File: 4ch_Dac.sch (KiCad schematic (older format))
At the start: 4 parts, among them J13 Conn_Coaxial, J14 Conn_Coaxial, J15 Conn_Coaxial, J16 Conn_Coaxial

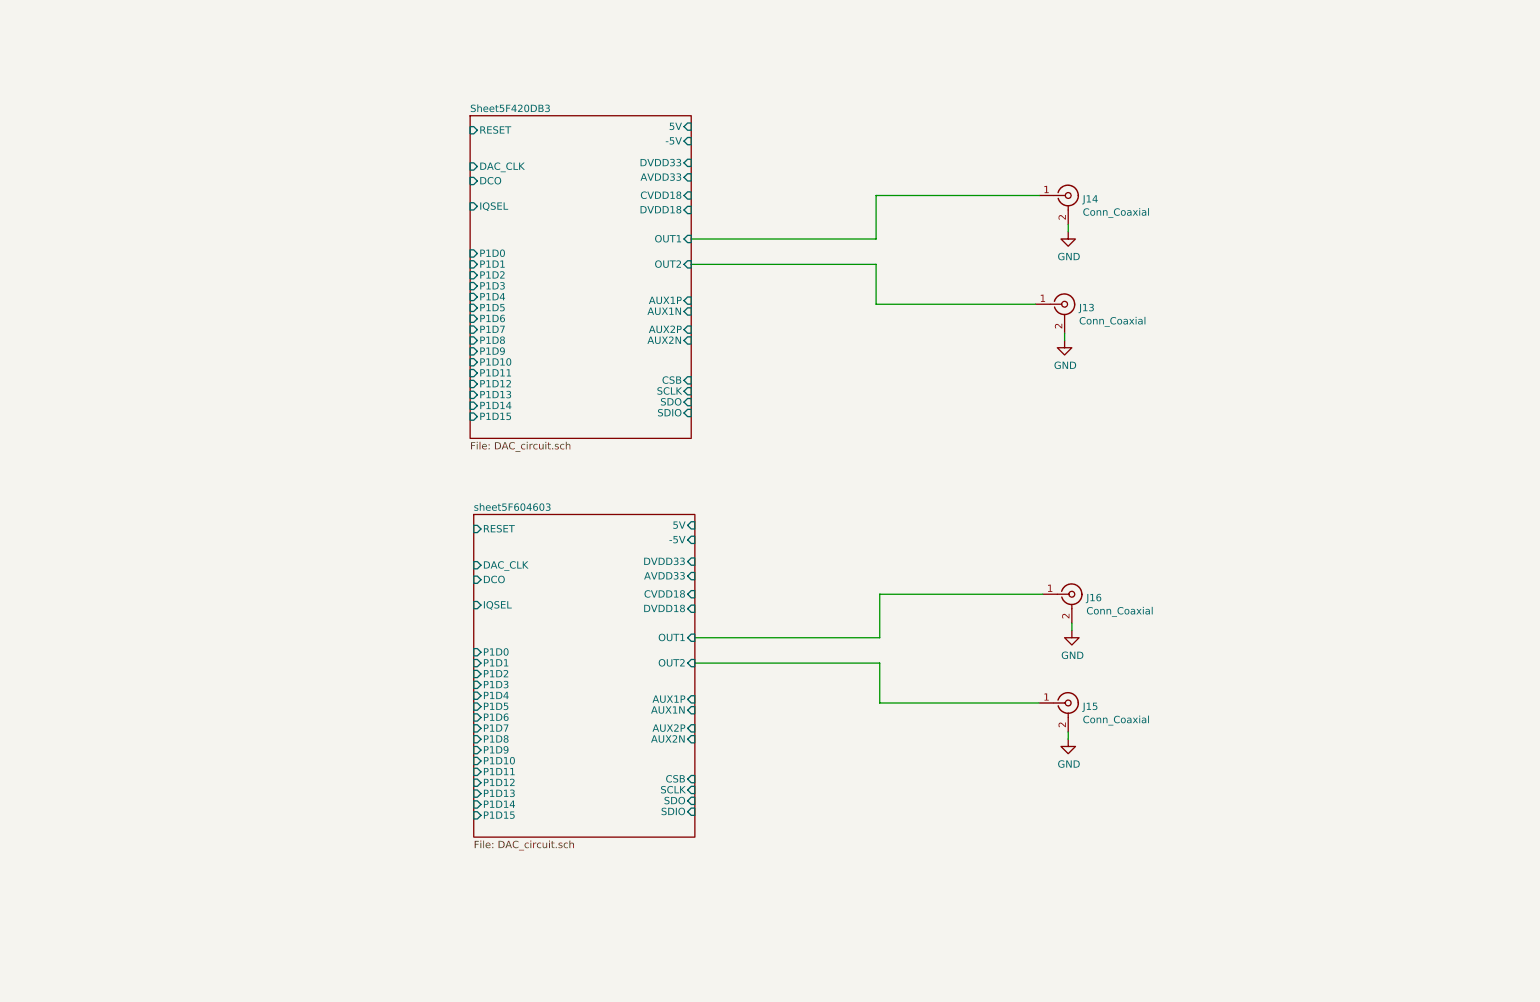
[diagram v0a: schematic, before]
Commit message: initial placement of all ADC/DAC blocks and added FPGA
Signed-off-by: Alexis Jeandet <alexis.jeandet@member.fsf.org>
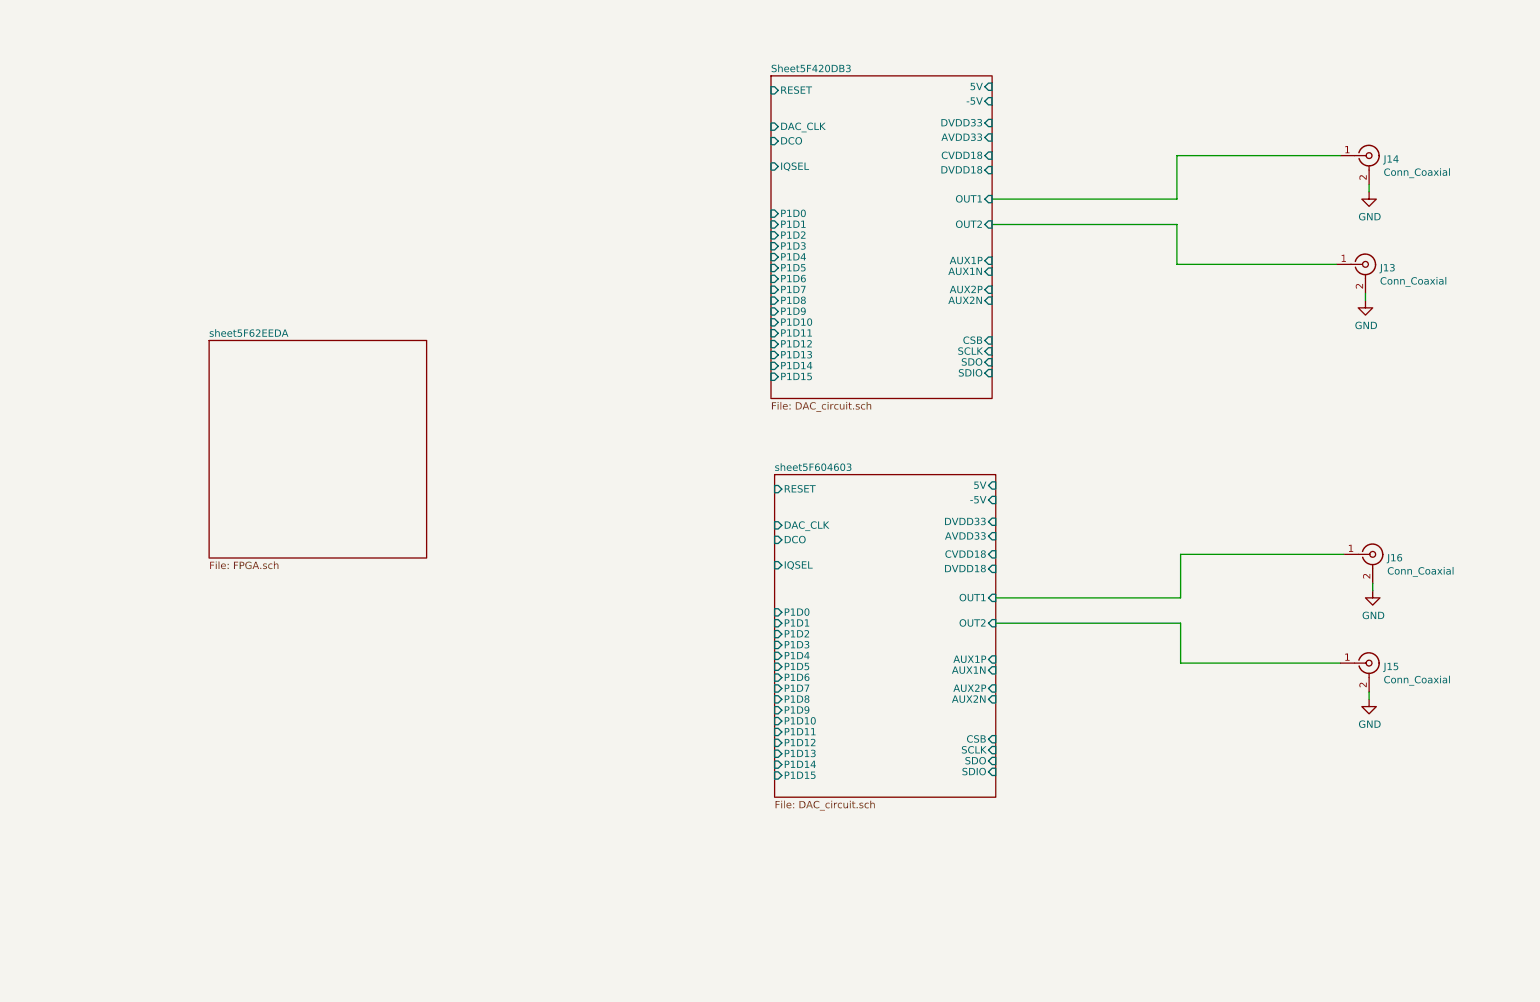
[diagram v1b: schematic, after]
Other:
- moved on the sheet: J13, J14, J15, J16

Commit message: Layout done for ADC + LVDS and DAC -> FPGA
Signed-off-by: Alexis Jeandet <alexis.jeandet@member.fsf.org>
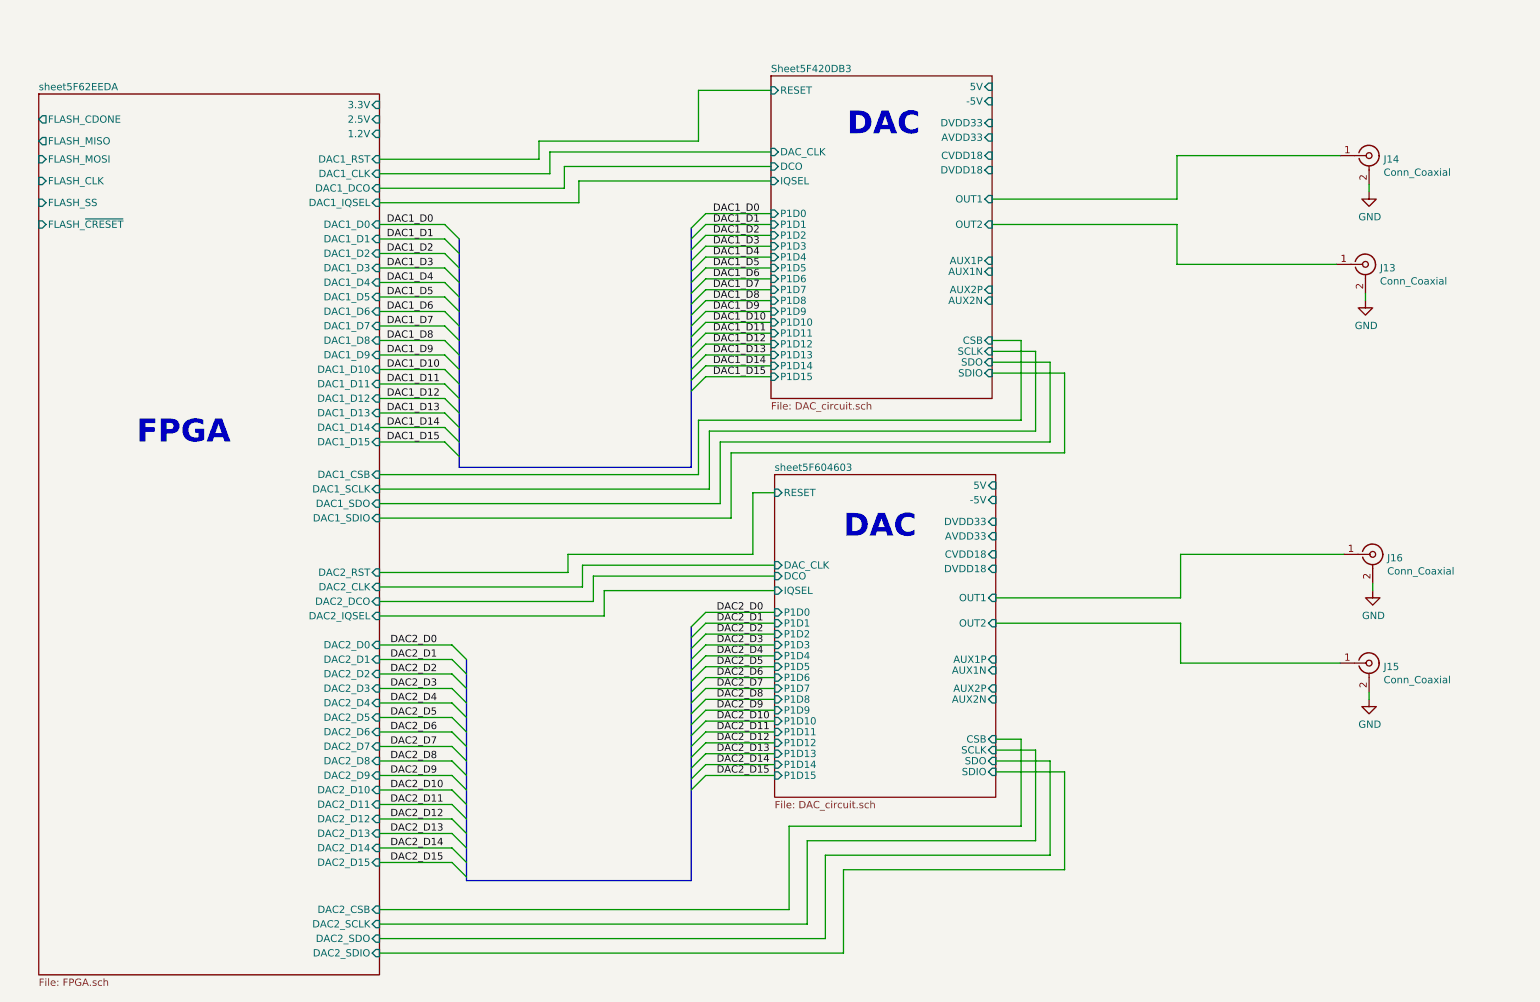
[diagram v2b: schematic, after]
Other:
- note added: "DAC"
- note added: "FPGA"

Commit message: Added #3.3V and #1.2V supply, completed ADC to USB board layout, added DAC FPGA to USB board bus.
Signed-off-by: Alexis Jeandet <alexis.jeandet@member.fsf.org>
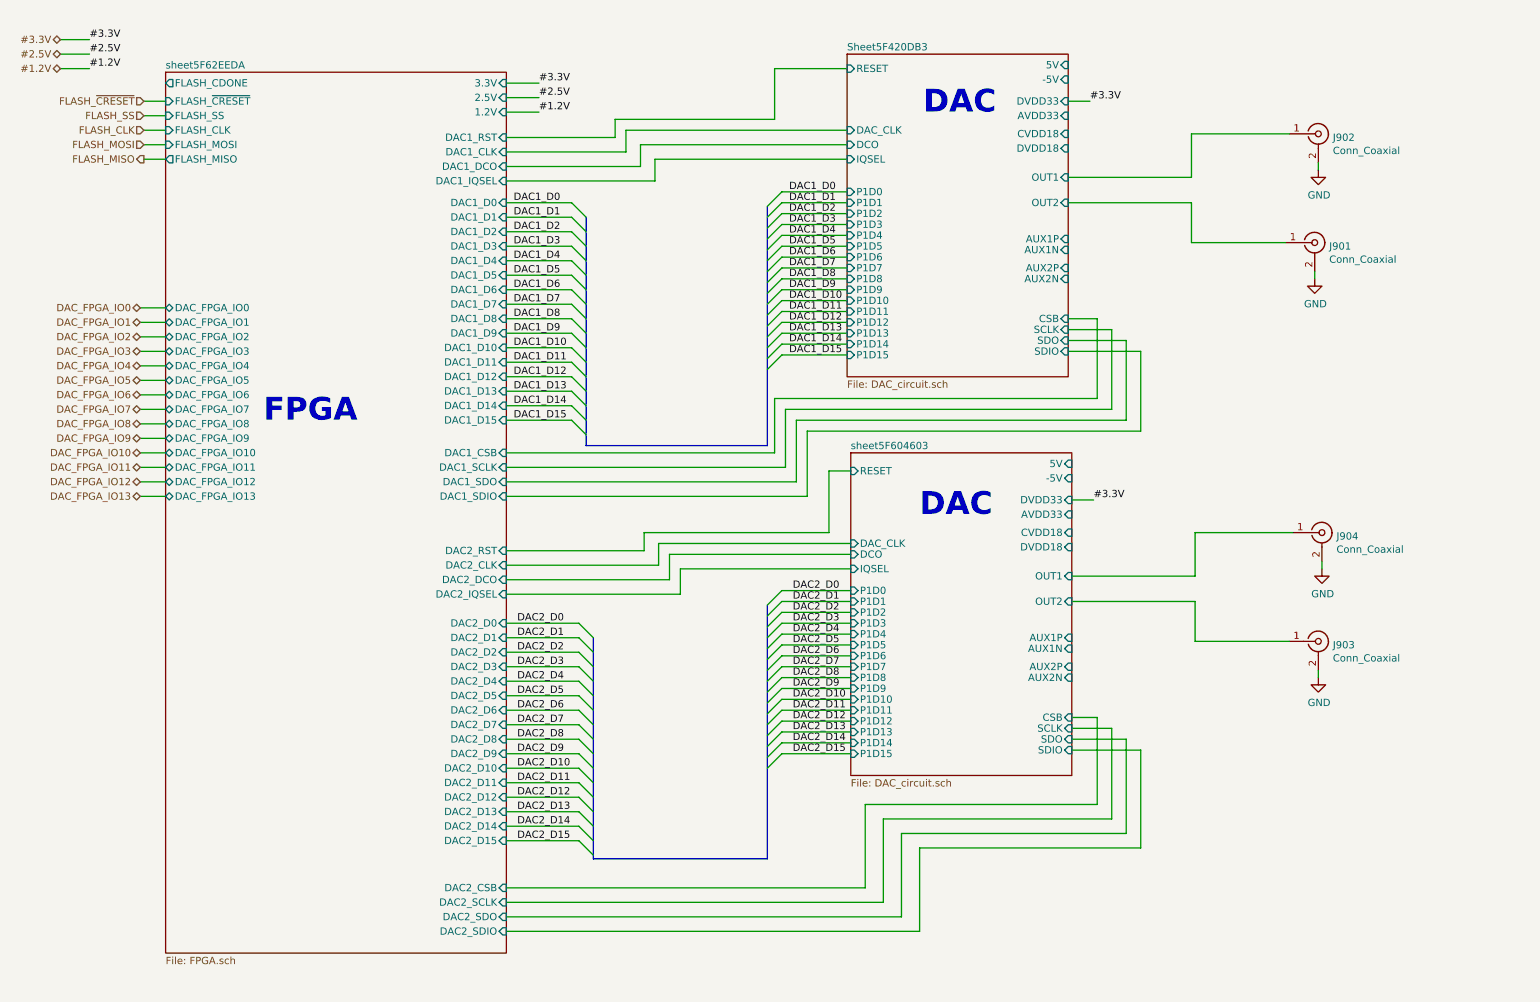
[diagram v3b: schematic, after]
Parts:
- renumbered J13 to J901, J14 to J902, J15 to J903, J16 to J904
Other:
- moved on the sheet: J901, J902, J903, J904

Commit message: Layout complete, needs silk screen cleanup and few checks
Signed-off-by: Alexis Jeandet <alexis.jeandet@member.fsf.org>
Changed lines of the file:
@@
 Wire Wire Line
 	1675 3850 1500 3850
-Text HLabel 950  700  0    50   BiDi ~ 0
+Text HLabel 10600 600  0    50   BiDi ~ 0
 #3.3V
-Text HLabel 950  800  0    50   BiDi ~ 0
+Text HLabel 10600 700  0    50   BiDi ~ 0
 #2.5V
-Text HLabel 950  900  0    50   BiDi ~ 0
+Text HLabel 10600 900  0    50   BiDi ~ 0
 #1.2V
 Wire Wire Line
-	950  700  1150 700
+	10600 600  10800 600
 Wire Wire Line
-	950  800  1150 800
+	10600 700  10800 700
 Wire Wire Line
-	950  900  1150 900
-Text Label 1150 700  0    50   ~ 0
+	10600 900  10800 900
+Text Label 10800 600  0    50   ~ 0
 #3.3V
-Text Label 1150 800  0    50   ~ 0
+Text Label 10800 700  0    50   ~ 0
 #2.5V
-Text Label 1150 900  0    50   ~ 0
+Text Label 10800 900  0    50   ~ 0
 #1.2V
 Text Label 4250 1000 0    50   ~ 0
@@
 Wire Wire Line
 	7900 1125 8050 1125
-Text Label 8075 3875 0    50   ~ 0
-#3.3V
-Wire Wire Line
-	7925 3875 8075 3875
 Text HLabel 1525 1525 0    50   Output ~ 0
 FLASH_MISO
@@
 Wire Wire Line
 	1675 1525 1525 1525
+Text Label 8125 1400 0    50   ~ 0
+#1.8V
+Wire Wire Line
+	7900 1350 8025 1350
+Wire Wire Line
+	8025 1350 8025 1400
+Wire Wire Line
+	8025 1450 7900 1450
+Wire Wire Line
+	8125 1400 8025 1400
+Connection ~ 8025 1400
+Wire Wire Line
+	8025 1400 8025 1450
+Text Label 8050 1225 0    50   ~ 0
+3.3V
+Wire Wire Line
+	8050 1225 7900 1225
+Text Label 8100 875  0    50   ~ 0
+5V
+Wire Wire Line
+	8100 875  7900 875
+Text Label 8100 975  0    50   ~ 0
+-5V
+Wire Wire Line
+	8100 975  7900 975
+Text Label 8075 3875 0    50   ~ 0
+#3.3V
+Wire Wire Line
+	7925 3875 8075 3875
+Text Label 8150 4150 0    50   ~ 0
+#1.8V
+Wire Wire Line
+	7925 4100 8050 4100
+Wire Wire Line
+	8050 4100 8050 4150
+Wire Wire Line
+	8050 4200 7925 4200
+Wire Wire Line
+	8150 4150 8050 4150
+Connection ~ 8050 4150
+Wire Wire Line
+	8050 4150 8050 4200
+Text Label 8075 3975 0    50   ~ 0
+3.3V
+Wire Wire Line
+	8075 3975 7925 3975
+Text Label 8125 3625 0    50   ~ 0
+5V
+Wire Wire Line
+	8125 3625 7925 3625
+Text Label 8125 3725 0    50   ~ 0
+-5V
+Wire Wire Line
+	8125 3725 7925 3725
+Text Label 10800 800  0    50   ~ 0
+#1.8V
+Text Label 10800 1200 0    50   ~ 0
+3.3V
+Text Label 10800 1000 0    50   ~ 0
+5V
+Text Label 10800 1100 0    50   ~ 0
+-5V
+Text HLabel 10600 800  0    50   BiDi ~ 0
+#1.8V
+Wire Wire Line
+	10600 800  10800 800
+Text HLabel 10600 1000 0    50   BiDi ~ 0
+5V
+Wire Wire Line
+	10600 1000 10800 1000
+Text HLabel 10600 1100 0    50   BiDi ~ 0
+-5V
+Wire Wire Line
+	10600 1100 10800 1100
+Text HLabel 10600 1200 0    50   BiDi ~ 0
+3.3V
+Wire Wire Line
+	10600 1200 10800 1200
 Wire Bus Line
 	4625 4825 4625 6350
